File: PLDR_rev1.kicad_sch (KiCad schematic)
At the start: 0 parts

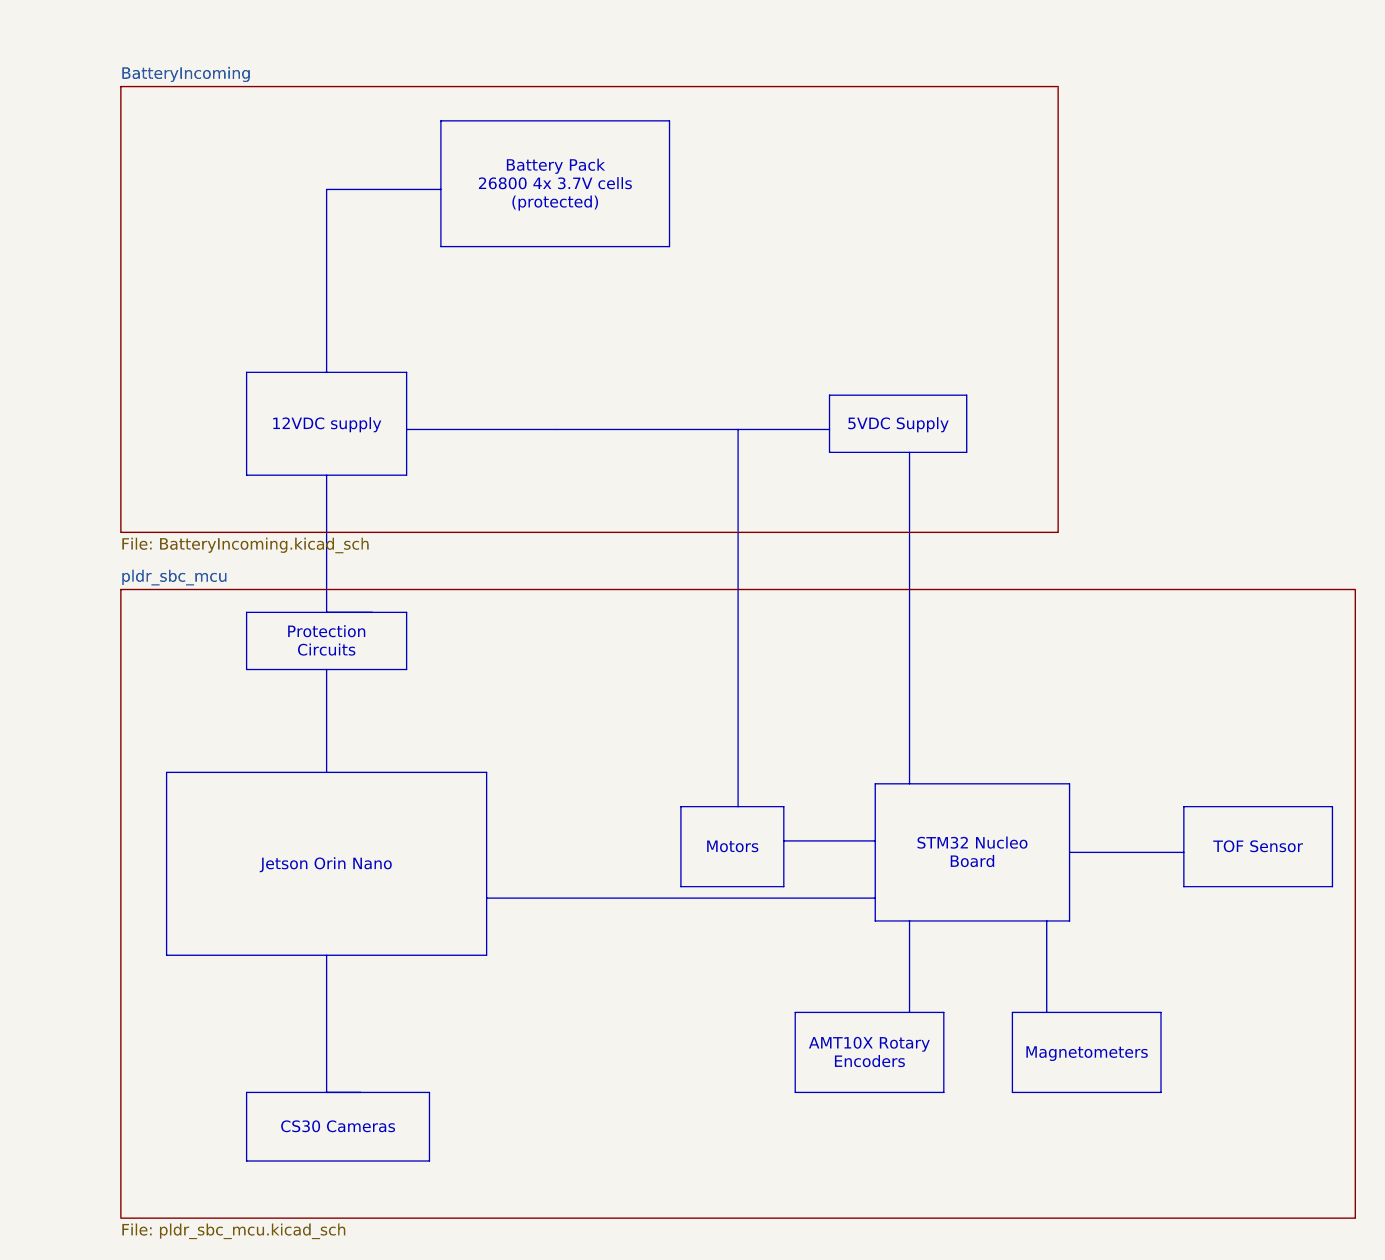
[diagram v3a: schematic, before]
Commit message: Implemented mcu/sensors/motors + modified info + modified .gitignore
- Confirmed pinouts on NUCLEO64-G474RE and routed them from dev board to
swerve drives
- Individual swerve drives (with/without TOF sensors) are Hierarchial
sheets
- .history was acting like a submodule and is not needed because we have
git so it was removed and its presence was added to .gitignore
- Added info on NC pins
- Still need confirmation on TBD pins + SPI signals
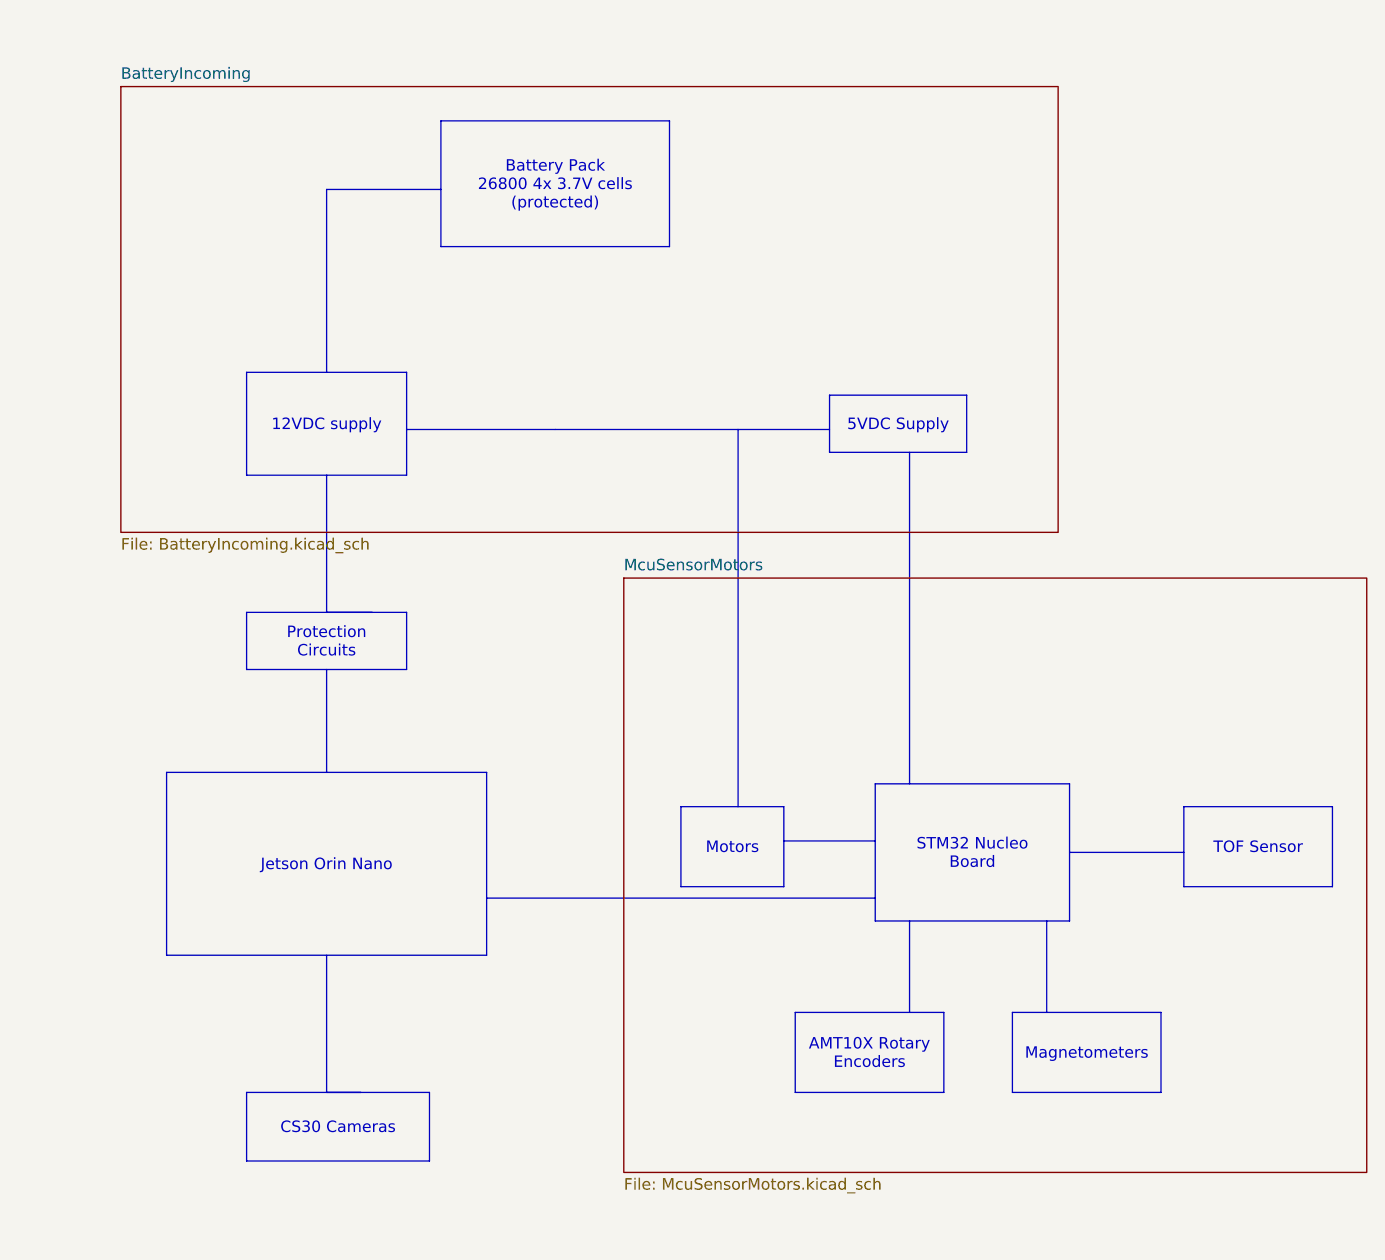
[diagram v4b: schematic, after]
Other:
- removed sheet pldr_sbc_mcu
- added sheet McuSensorMotors (McuSensorMotors.kicad_sch)
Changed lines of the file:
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@@
 	)
 	(sheet
-		(at 49.53 82.55)
-		(size 137.16 69.85)
+		(at 105.41 81.28)
+		(size 82.55 66.04)
 		(exclude_from_sim no)
 		(in_bom yes)
@@
 			(color 0 0 0 0)
 		)
-		(property "Sheetname" "pldr_sbc_mcu"
-			(at 49.53 81.8384 0)
+		(property "Sheetname" "McuSensorMotors"
+			(at 105.41 80.5684 0)
 			(show_name no)
 			(do_not_autoplace no)
@@
 			)
 		)
-		(property "Sheetfile" "pldr_sbc_mcu.kicad_sch"
-			(at 49.53 152.9846 0)
+		(property "Sheetfile" "McuSensorMotors.kicad_sch"
+			(at 105.41 147.9046 0)
 			(show_name no)
 			(do_not_autoplace no)
